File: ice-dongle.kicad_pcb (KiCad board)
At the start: 2 copper layers, 43 parts, among them J1 USB4155-03-C_REVA, J2 NC Jumper, J3 PROG HEADER, J4 FFC2B35-18-G_REVA2, SW1 SW_Push, SW2 SW_Push, U1 APS6404L-3SQR, U2 W25Q64JWUUIQ, U3 DRTR5V0U4S, U4 MCP1824x-OT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

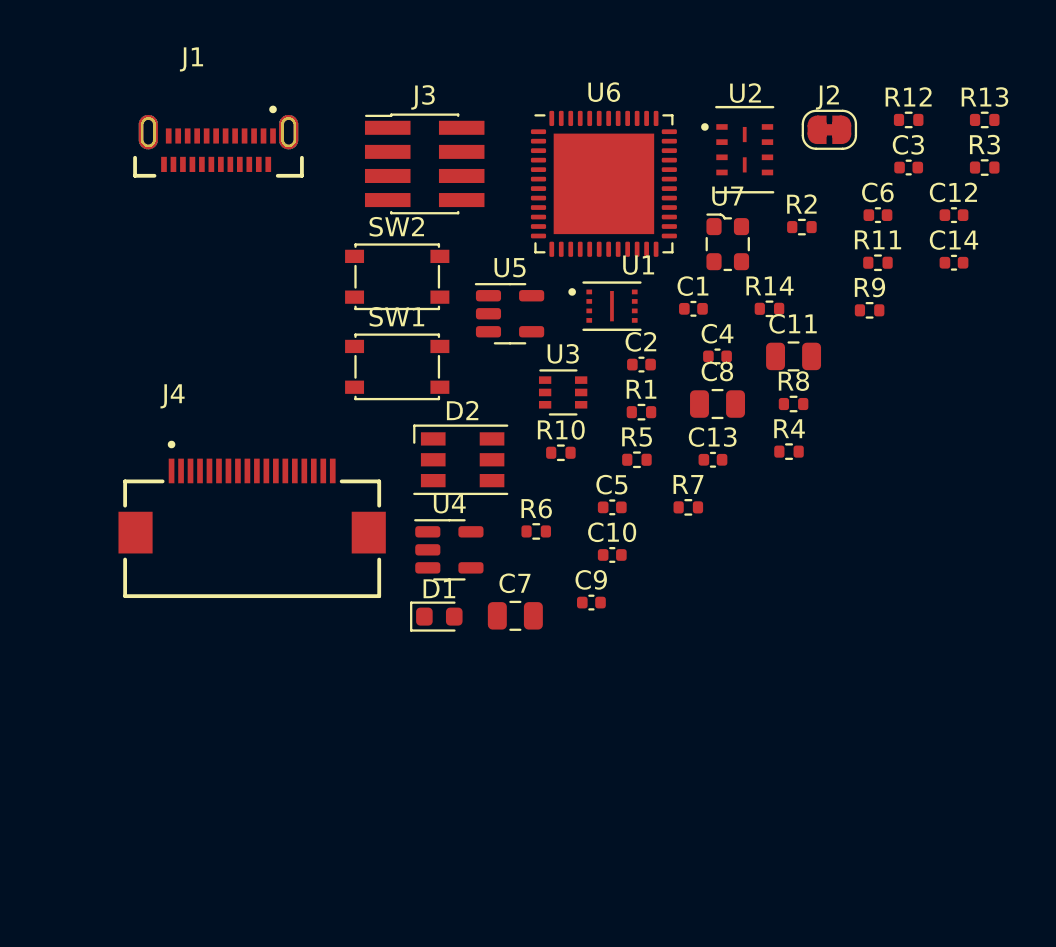
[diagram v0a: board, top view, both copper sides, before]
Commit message: USB-C jack, finish layout
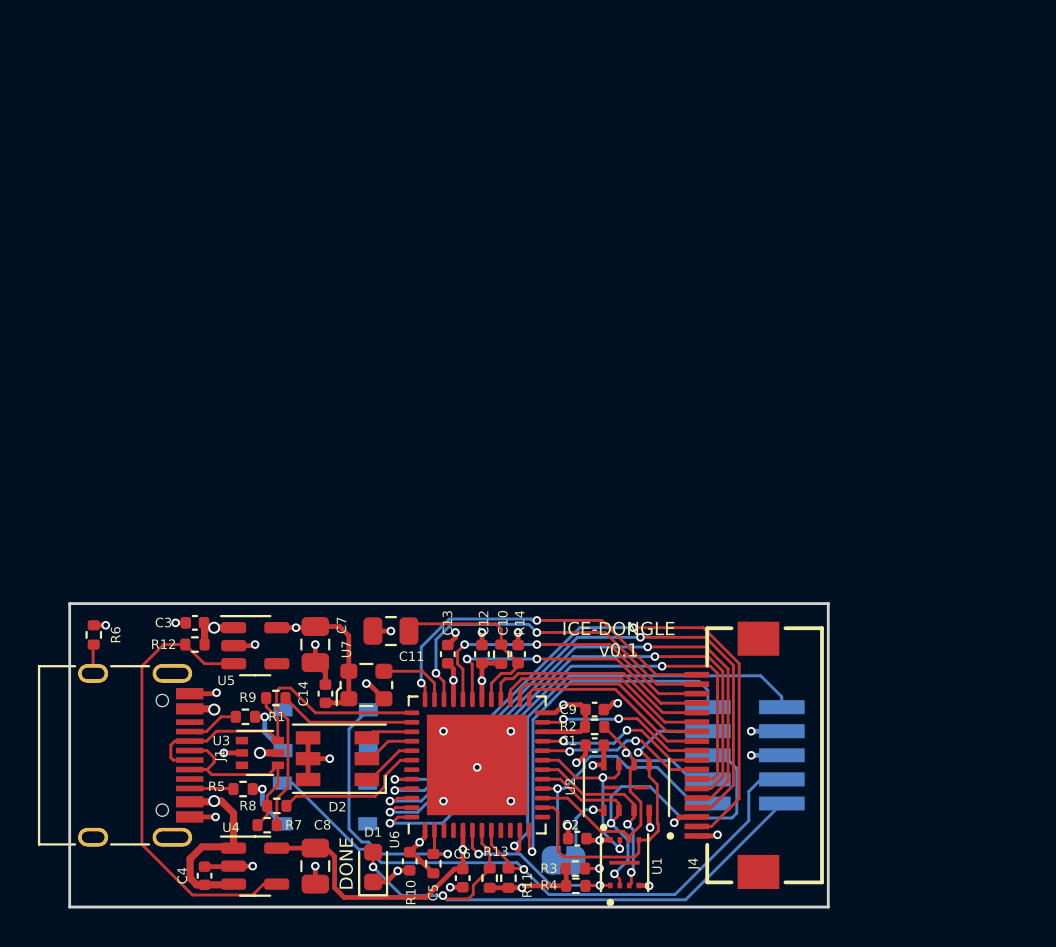
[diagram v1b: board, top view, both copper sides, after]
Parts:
- added Ref**: Val**, emeb_library:avatar_small, B.Cu at (125.9, 105.7)
- J1: value USB4155-03-C_REVA -> USB_C_Receptacle_USB2.0; footprint emeb_library:GCT_USB4155-03-C_REVA -> Connector_USB:USB_C_Receptacle_HRO_TYPE-C-31-M-12
- J2, SW1, SW2: moved to B.Cu
- J3: footprint Connector_PinHeader_1.27mm:PinHeader_2x04_P1.27mm_Vertical_SMD -> Connector_PinHeader_1.27mm:PinHeader_2x05_P1.27mm_Vertical_SMD; moved to B.Cu
- moved R13 47.7 mm to (123.7, 116.1), turned to 90 degrees
- moved R12 46.7 mm to (108.2, 103.8)
- moved C3 44.6 mm to (108.2, 102.6), turned to 180 degrees
- moved R3 42.8 mm to (128.3, 115.6)
- moved C6 41.3 mm to (122.3, 116.1), turned to -90 degrees
- moved J2 41.0 mm to (127.6, 115.1)
- moved C14 40.2 mm to (115.1, 106.3), turned to 90 degrees
- moved C4 38.5 mm to (108.7, 116.0), turned to 90 degrees
- moved R11 37.9 mm to (124.7, 116.1), turned to 90 degrees
- moved R9 37.4 mm to (112.5, 106.6), turned to 180 degrees
- moved J3 35.5 mm to (137.2, 109.6)
- moved R8 34.5 mm to (112.5, 112.3), turned to 180 degrees
- moved U2 34.2 mm to (131.0, 111.3), turned to 90 degrees
- moved C12 34.0 mm to (123.3, 104.3), turned to 90 degrees
- moved J1 32.4 mm to (103.9, 109.6), turned to -90 degrees
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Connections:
- net +3V3 renamed +3.3V
- R1 pad 1: Net-(J1-PadA5) -> GND
- R1 pad 2: GND -> Net-(J1-PadA5)
- R6 pad 1: Net-(J1-PadS1) -> GND
- R6 pad 2: GND -> Net-(J1-PadS1)
- U6 pad 11: unconnected-(U6-Pad11) -> /SPARE10
- U6 pad 12: unconnected-(U6-Pad12) -> /SPARE9
- U6 pad 20: unconnected-(U6-Pad20) -> /ES_RST
- U6 pad 21: /ES_P18 -> /ES_TFTCS
- U6 pad 23: /ES_P17 -> /ES_SDCS
- U6 pad 25: /ES_P16 -> /ES_P11
- U6 pad 26: /ES_P15 -> /ES_P12
- U6 pad 27: /ES_P14 -> /ES_P13
- U6 pad 28: /ES_P13 -> /ES_P14
- U6 pad 31: /ES_P12 -> /ES_P15
- U6 pad 32: /ES_P11 -> /ES_P16
- U6 pad 34: /ES_SDCS -> /ES_P17
- U6 pad 36: /ES_TFTCS -> /ES_P18
- U6 pad 43: /ES_RST -> unconnected-(U6-Pad43)
- U6 pad 44: /ES_DC -> /ES_BKL
- U6 pad 45: /ES_POCI -> /ES_SCK
- U6 pad 47: /ES_SCK -> /ES_POCI
- U6 pad 48: /ES_BKL -> /ES_DC
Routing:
- net /~{CRESET}: track 0.00 -> 35.5 mm, vias 0 -> 1
- net +3.3V: track 0.00 -> 33.8 mm, vias 0 -> 10
- net /ES_BKL: track 0.00 -> 33.1 mm, vias 0 -> 2
- net GND: track 0.00 -> 31.8 mm, vias 0 -> 30
- net /ES_SCK: track 0.00 -> 31.5 mm, vias 0 -> 2
- net /ES_PICO: track 0.00 -> 30.8 mm, vias 0 -> 2
- net /CDONE: track 0.00 -> 30.8 mm, vias 0 -> 2
- net /ES_POCI: track 0.00 -> 29.7 mm, vias 0 -> 2
- net /ES_DC: track 0.00 -> 29.5 mm, vias 0 -> 2
- net /VUSB: track 0.00 -> 28.0 mm, vias 0 -> 4
- net +1V2: track 0.00 -> 26.8 mm, vias 0 -> 2
- net /SPARE10: track 0.00 -> 23.9 mm, vias 0 -> 1
- net /PGOOD_1.2: track 0.00 -> 23.6 mm
- net /MEM_SPI_POCI-IO1: track 0.00 -> 23.1 mm, vias 0 -> 2
- net /SPARE9: track 0.00 -> 19.3 mm, vias 0 -> 1
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- added copper zone on In2.Cu, net +3.3V
- added copper zone on In1.Cu, net GND
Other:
- board outline added: 40 x 16 mm
- copper layers 2 -> 4
- rule pad_to_mask_clearance: 0 -> 0.051
- board text added: "BOOT"
- board text added: "CI"
- board text added: "CK"
- board text added: "CO"
- board text added: "CS"
- board text added: "D"
- board text added: "DONE"
- board text added: "FLASH CS"
- board text added: "G"
- board text added: "ICE-DONGLE v0.1"
- board text added: "ICE-DONGLE v0.1 (c)2022 E. Brombaugh"
- board text added: "PRG HDR"
- board text added: "R"
- board text added: "RST"
- board text added: "V"

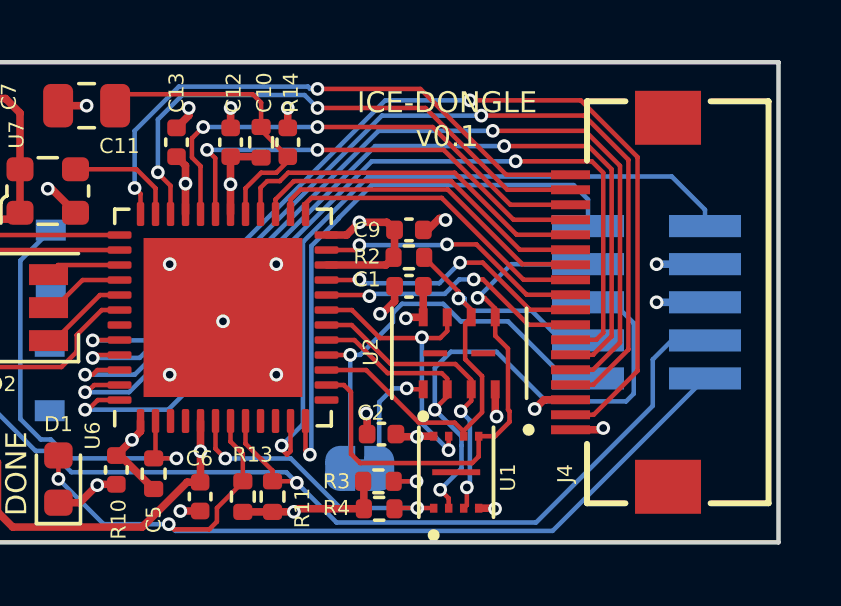
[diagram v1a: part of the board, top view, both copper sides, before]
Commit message: Fix Eye-SPI pinout, add VIN selector
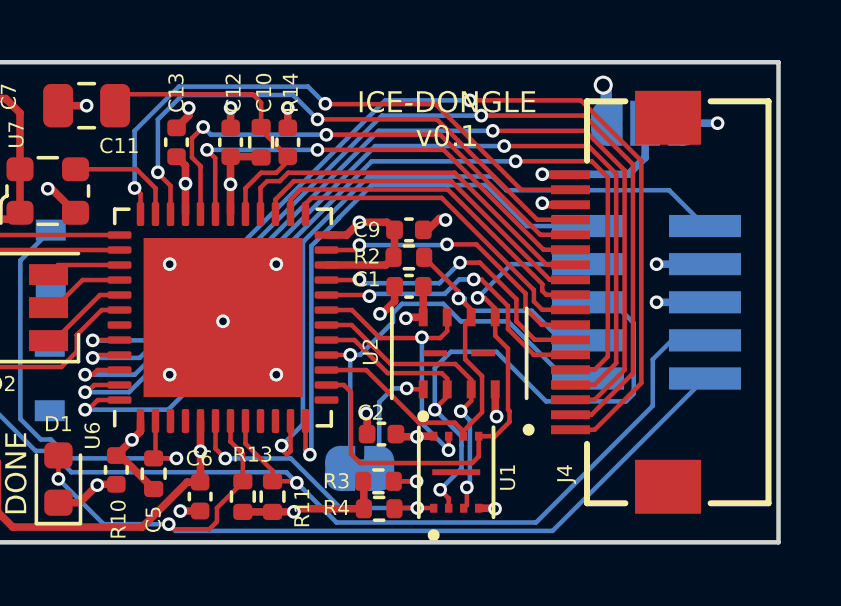
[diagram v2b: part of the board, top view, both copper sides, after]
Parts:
- added JP1: Jumper_3_Bridged12, Jumper:SolderJumper-3_P1.3mm_Bridged12_RoundedPad1.0x1.5mm, B.Cu at (137.2, 103.6)
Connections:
- J4 pad 1: +3.3V -> /ES_GP2
- J4 pad 10: /ES_SDCS -> /ES_TFTCS
- J4 pad 11: /ES_P11 -> /ES_RST
- J4 pad 12: /ES_P12 -> /ES_DC
- J4 pad 13: /ES_P13 -> /ES_POCI
- J4 pad 14: /ES_P14 -> /ES_PICO
- J4 pad 15: /ES_P15 -> /ES_SCK
- J4 pad 16: /ES_P16 -> GND
- J4 pad 17: /ES_P17 -> /ES_BKL
- J4 pad 18: /ES_P18 -> /ES_VIN
- J4 pad 2: /ES_BKL -> /ES_GP1
- J4 pad 3: GND -> /ES_BUSY
- J4 pad 4: /ES_SCK -> /ES_INT
- J4 pad 5: /ES_PICO -> /ES_SDA
- J4 pad 6: /ES_POCI -> /ES_SCL
- J4 pad 7: /ES_DC -> /ES_TSCS
- J4 pad 8: /ES_RST -> /ES_MEMCS
- J4 pad 9: /ES_TFTCS -> /ES_SDCS
- U6 pad 20: /ES_RST -> /ES_SCL
- U6 pad 21: /ES_TFTCS -> /ES_TSCS
- U6 pad 23: /ES_SDCS -> /ES_MEMCS
- U6 pad 25: /ES_P11 -> /ES_SDCS
- U6 pad 26: /ES_P12 -> /ES_TFTCS
- U6 pad 27: /ES_P13 -> /ES_RST
- U6 pad 28: /ES_P14 -> /ES_DC
- U6 pad 31: /ES_P15 -> /ES_POCI
- U6 pad 32: /ES_P16 -> /ES_PICO
- U6 pad 34: /ES_P17 -> /ES_SCK
- U6 pad 36: /ES_P18 -> /ES_BKL
- U6 pad 44: /ES_BKL -> /ES_GP2
- U6 pad 45: /ES_SCK -> /ES_GP1
- U6 pad 46: /ES_PICO -> /ES_BUSY
- U6 pad 47: /ES_POCI -> /ES_INT
- U6 pad 48: /ES_DC -> /ES_SDA
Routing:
- net /ES_GP2: track 0.00 -> 33.7 mm, vias 0 -> 2
- net /ES_GP1: track 0.00 -> 32.6 mm, vias 0 -> 2
- net /ES_BUSY: track 0.00 -> 32.0 mm, vias 0 -> 2
- net /ES_INT: track 0.00 -> 30.9 mm, vias 0 -> 2
- net /ES_SDA: track 0.00 -> 30.6 mm, vias 0 -> 2
- net /VUSB: track 28.0 -> 56.1 mm, vias 4 -> 5
- net /ES_P18: track 19.2 -> 0.00 mm, vias 2 -> 0
- net /ES_P17: track 18.7 -> 0.00 mm, vias 2 -> 0
- net /ES_DC: track 29.5 -> 12.7 mm, vias 2 -> 0
- net /ES_P16: track 16.5 -> 0.00 mm, vias 2 -> 0
- net /ES_P15: track 15.3 -> 0.00 mm, vias 2 -> 0
- net /ES_POCI: track 29.7 -> 15.8 mm
- net /ES_PICO: track 30.8 -> 16.9 mm
- net /ES_BKL: track 33.1 -> 19.4 mm
- net /ES_SCK: track 31.5 -> 19.2 mm
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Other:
- board text added: "3v3"
- board text added: "VBUS"

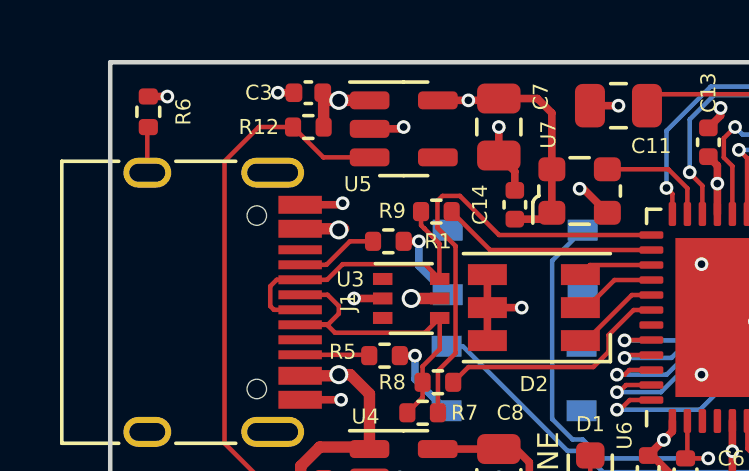
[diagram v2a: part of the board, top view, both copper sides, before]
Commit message: Fix issues pointed out by @m_w, update image
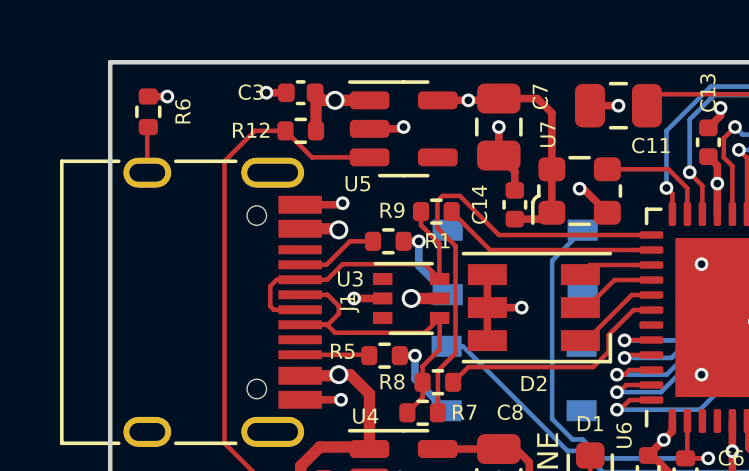
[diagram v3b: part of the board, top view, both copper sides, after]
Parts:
- moved R12 0.28 mm to (108.0, 103.9)
- moved C3 0.25 mm to (108.0, 102.6)
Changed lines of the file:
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@@
   )
   (footprint "Resistor_SMD:R_0402_1005Metric" (layer "F.Cu")
-    (at 108.204 103.759)
+    (at 107.95 103.886)
     (descr "Resistor SMD 0402 (1005 Metric), square (rectangular) end terminal, IPC_7351 nominal, (Body size source: IPC-SM-782 page 72, https://www.pcb-3d.com/wordpress/wp-content/uploads/ipc-sm-782a_amendment_1_and_2.pdf), generated with kicad-footprint-generator")
     (tags "resistor")
@@
   )
   (footprint "Capacitor_SMD:C_0402_1005Metric" (layer "F.Cu")
-    (at 108.204 102.616 180)
+    (at 107.95 102.616 180)
     (descr "Capacitor SMD 0402 (1005 Metric), square (rectangular) end terminal, IPC_7351 nominal, (Body size source: IPC-SM-782 page 76, https://www.pcb-3d.com/wordpress/wp-content/uploads/ipc-sm-782a_amendment_1_and_2.pdf), generated with kicad-footprint-generator")
     (tags "capacitor")
@@
   (segment (start 118.3132 116.2812) (end 118.8974 115.697) (width 0.254) (layer "F.Cu") (net 2))
   (segment (start 108.712 115.471) (end 110.2135 115.471) (width 0.254) (layer "F.Cu") (net 2))
-  (segment (start 107.724 102.616) (end 107.188 102.616) (width 0.254) (layer "F.Cu") (net 2))
   (segment (start 114.554 116.393) (end 114.554 115.443) (width 0.254) (layer "F.Cu") (net 2))
   (segment (start 110.683 109.474) (end 109.728 109.474) (width 0.254) (layer "F.Cu") (net 2))
@@
   (segment (start 127.8916 113.9952) (end 127.8916 113.312) (width 0.254) (layer "F.Cu") (net 2))
   (segment (start 115.0874 105.2424) (end 114.554 104.709) (width 0.254) (layer "F.Cu") (net 2))
+  (segment (start 107.47 102.616) (end 106.807 102.616) (width 0.254) (layer "F.Cu") (net 2))
   (segment (start 117.3702 105.8164) (end 118.1714 106.6176) (width 0.254) (layer "F.Cu") (net 2))
   (segment (start 129.921 107.188) (end 130.302 106.807) (width 0.254) (layer "F.Cu") (net 2))
@@
   (via (at 111.379 103.759) (size 0.4572) (drill 0.254) (layers "F.Cu" "B.Cu") (net 2))
   (via (at 117.2464 105.8164) (size 0.4572) (drill 0.254) (layers "F.Cu" "B.Cu") (net 2))
-  (via (at 107.188 102.616) (size 0.4572) (drill 0.254) (layers "F.Cu" "B.Cu") (net 2))
+  (via (at 106.807 102.616) (size 0.4572) (drill 0.254) (layers "F.Cu" "B.Cu") (net 2))
   (via (at 111.76 111.379) (size 0.4572) (drill 0.254) (layers "F.Cu" "B.Cu") (net 2))
   (via (at 118.5418 103.0478) (size 0.4572) (drill 0.254) (layers "F.Cu" "B.Cu") (net 2))
@@
   (segment (start 111.76 111.379) (end 111.76 112.164) (width 0.254) (layer "B.Cu") (net 2))
   (segment (start 107.95 115.062) (end 108.585 114.427) (width 0.381) (layer "F.Cu") (net 3))
-  (segment (start 108.714 103.759) (end 108.714 102.646) (width 0.381) (layer "F.Cu") (net 3))
-  (segment (start 110.247 102.87) (end 108.938 102.87) (width 0.381) (layer "F.Cu") (net 3))
   (segment (start 111.633 109.474) (end 112.583 109.474) (width 0.381) (layer "F.Cu") (net 3))
   (segment (start 109.22 112.014) (end 109.601 112.014) (width 0.381) (layer "F.Cu") (net 3))
@@
   (segment (start 108.712 116.431) (end 110.2035 116.431) (width 0.381) (layer "F.Cu") (net 3))
   (segment (start 110.2035 116.431) (end 110.2415 116.393) (width 0.381) (layer "F.Cu") (net 3))
-  (segment (start 108.714 102.646) (end 108.684 102.616) (width 0.381) (layer "F.Cu") (net 3))
+  (segment (start 109.183 107.151) (end 109.22 107.188) (width 0.381) (layer "F.Cu") (net 3))
   (segment (start 109.183 112.051) (end 109.22 112.014) (width 0.381) (layer "F.Cu") (net 3))
   (segment (start 107.931 112.051) (end 109.183 112.051) (width 0.381) (layer "F.Cu") (net 3))
-  (segment (start 107.931 107.151) (end 109.384 107.151) (width 0.381) (layer "F.Cu") (net 3))
+  (segment (start 110.247 102.87) (end 108.684 102.87) (width 0.381) (layer "F.Cu") (net 3))
+  (segment (start 108.684 102.87) (end 108.43 102.616) (width 0.381) (layer "F.Cu") (net 3))
   (segment (start 110.1755 114.427) (end 110.2415 114.493) (width 0.381) (layer "F.Cu") (net 3))
   (segment (start 107.95 116.078) (end 107.95 115.062) (width 0.381) (layer "F.Cu") (net 3))
-  (segment (start 108.938 102.87) (end 108.684 102.616) (width 0.381) (layer "F.Cu") (net 3))
+  (segment (start 108.46 103.886) (end 108.46 102.646) (width 0.381) (layer "F.Cu") (net 3))
   (segment (start 110.2415 112.6545) (end 110.2415 114.493) (width 0.381) (layer "F.Cu") (net 3))
   (segment (start 109.601 112.014) (end 110.2415 112.6545) (width 0.381) (layer "F.Cu") (net 3))
+  (segment (start 107.931 107.151) (end 109.183 107.151) (width 0.381) (layer "F.Cu") (net 3))
+  (segment (start 108.46 102.646) (end 108.43 102.616) (width 0.381) (layer "F.Cu") (net 3))
   (segment (start 108.303 116.431) (end 107.95 116.078) (width 0.381) (layer "F.Cu") (net 3))
   (via (at 111.633 109.474) (size 0.635) (drill 0.4318) (layers "F.Cu" "B.Cu") (net 3))
   (via (at 135.763 102.362) (size 0.635) (drill 0.4318) (layers "F.Cu" "B.Cu") (net 3))
-  (via (at 109.22 102.87) (size 0.635) (drill 0.4318) (layers "F.Cu" "B.Cu") (net 3))
+  (via (at 109.093 102.87) (size 0.635) (drill 0.4318) (layers "F.Cu" "B.Cu") (net 3))
   (via (at 109.22 112.014) (size 0.635) (drill 0.4318) (layers "F.Cu" "B.Cu") (net 3))
   (via (at 109.22 107.188) (size 0.635) (drill 0.4318) (layers "F.Cu" "B.Cu") (net 3))
+  (segment (start 109.6391 102.3239) (end 135.7249 102.3239) (width 0.381) (layer "In2.Cu") (net 3))
   (segment (start 110.8329 110.2741) (end 111.633 109.474) (width 0.381) (layer "In2.Cu") (net 3))
-  (segment (start 108.8009 103.2891) (end 109.22 102.87) (width 0.381) (layer "In2.Cu") (net 3))
-  (segment (start 108.8009 106.7689) (end 108.8009 103.2891) (width 0.381) (layer "In2.Cu") (net 3))
-  (segment (start 109.22 107.188) (end 108.8009 106.7689) (width 0.381) (layer "In2.Cu") (net 3))
+  (segment (start 108.8009 103.1621) (end 108.8009 106.7689) (width 0.381) (layer "In2.Cu") (net 3))
   (segment (start 109.1819 111.9759) (end 109.1819 110.2741) (width 0.381) (layer "In2.Cu") (net 3))
-  (segment (start 109.7661 102.3239) (end 135.7249 102.3239) (width 0.381) (layer "In2.Cu") (net 3))
   (segment (start 109.1819 107.2261) (end 109.22 107.188) (width 0.381) (layer "In2.Cu") (net 3))
+  (segment (start 108.8009 106.7689) (end 109.22 107.188) (width 0.381) (layer "In2.Cu") (net 3))
   (segment (start 109.22 112.014) (end 109.1819 111.9759) (width 0.381) (layer "In2.Cu") (net 3))
+  (segment (start 135.7249 102.3239) (end 135.763 102.362) (width 0.381) (layer "In2.Cu") (net 3))
   (segment (start 109.1819 110.2741) (end 109.1819 107.2261) (width 0.381) (layer "In2.Cu") (net 3))
-  (segment (start 109.22 102.87) (end 109.7661 102.3239) (width 0.381) (layer "In2.Cu") (net 3))
-  (segment (start 135.7249 102.3239) (end 135.763 102.362) (width 0.381) (layer "In2.Cu") (net 3))
+  (segment (start 109.093 102.87) (end 108.8009 103.1621) (width 0.381) (layer "In2.Cu") (net 3))
   (segment (start 109.1819 110.2741) (end 110.8329 110.2741) (width 0.381) (layer "In2.Cu") (net 3))
+  (segment (start 109.093 102.87) (end 109.6391 102.3239) (width 0.381) (layer "In2.Cu") (net 3))
   (segment (start 135.86 102.459) (end 135.763 102.362) (width 0.381) (layer "B.Cu") (net 3))
   (segment (start 135.86 103.632) (end 135.86 102.459) (width 0.381) (layer "B.Cu") (net 3))
@@
   (segment (start 117.0126 114.173) (end 116.332 113.4924) (width 0.1524) (layer "B.Cu") (net 45))
   (segment (start 116.332 113.4924) (end 116.332 108.213) (width 0.1524) (layer "B.Cu") (net 45))
+  (segment (start 106.426 103.886) (end 107.44 103.886) (width 0.1524) (layer "F.Cu") (net 46))
+  (segment (start 111.826 116.393) (end 111.252 116.967) (width 0.1524) (layer "F.Cu") (net 46))
+  (segment (start 108.077 116.967) (end 105.41 114.3) (width 0.1524) (layer "F.Cu") (net 46))
+  (segment (start 108.324 104.77) (end 107.44 103.886) (width 0.1524) (layer "F.Cu") (net 46))
+  (segment (start 105.41 114.3) (end 105.41 104.902) (width 0.1524) (layer "F.Cu") (net 46))
+  (segment (start 110.247 104.77) (end 108.324 104.77) (width 0.1524) (layer "F.Cu") (net 46))
+  (segment (start 111.252 116.967) (end 108.077 116.967) (width 0.1524) (layer "F.Cu") (net 46))
   (segment (start 112.5165 116.393) (end 111.826 116.393) (width 0.1524) (layer "F.Cu") (net 46))
-  (segment (start 105.41 114.3) (end 105.41 104.902) (width 0.1524) (layer "F.Cu") (net 46))
-  (segment (start 108.705 104.77) (end 107.694 103.759) (width 0.1524) (layer "F.Cu") (net 46))
-  (segment (start 108.077 116.967) (end 105.41 114.3) (width 0.1524) (layer "F.Cu") (net 46))
-  (segment (start 111.826 116.393) (end 111.252 116.967) (width 0.1524) (layer "F.Cu") (net 46))
-  (segment (start 105.41 104.902) (end 106.553 103.759) (width 0.1524) (layer "F.Cu") (net 46))
-  (segment (start 110.247 104.77) (end 108.705 104.77) (width 0.1524) (layer "F.Cu") (net 46))
-  (segment (start 111.252 116.967) (end 108.077 116.967) (width 0.1524) (layer "F.Cu") (net 46))
-  (segment (start 106.553 103.759) (end 107.694 103.759) (width 0.1524) (layer "F.Cu") (net 46))
+  (segment (start 105.41 104.902) (end 106.426 103.886) (width 0.1524) (layer "F.Cu") (net 46))
   (segment (start 128.6764 111.6584) (end 130.8354 111.6584) (width 0.1524) (layer "F.Cu") (net 47))
   (segment (start 131.2164 116.3596) (end 131.1108 116.4652) (width 0.1524) (layer "F.Cu") (net 47))
